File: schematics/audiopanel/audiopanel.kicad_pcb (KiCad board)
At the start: 2 copper layers, 29.2 x 21.6 mm, 3 parts, among them J1 Audio IN, J2 Audio OUT, J3 Conn

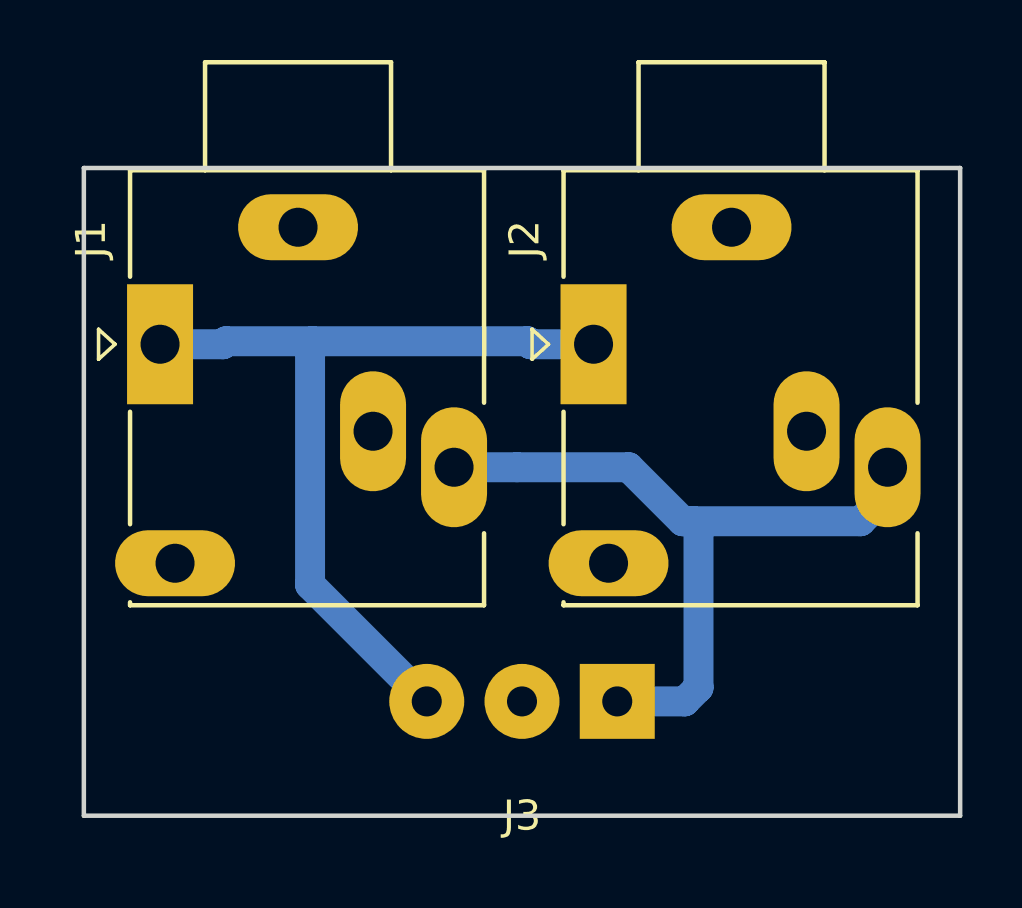
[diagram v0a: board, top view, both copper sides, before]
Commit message: Updated PCB for audio connectors
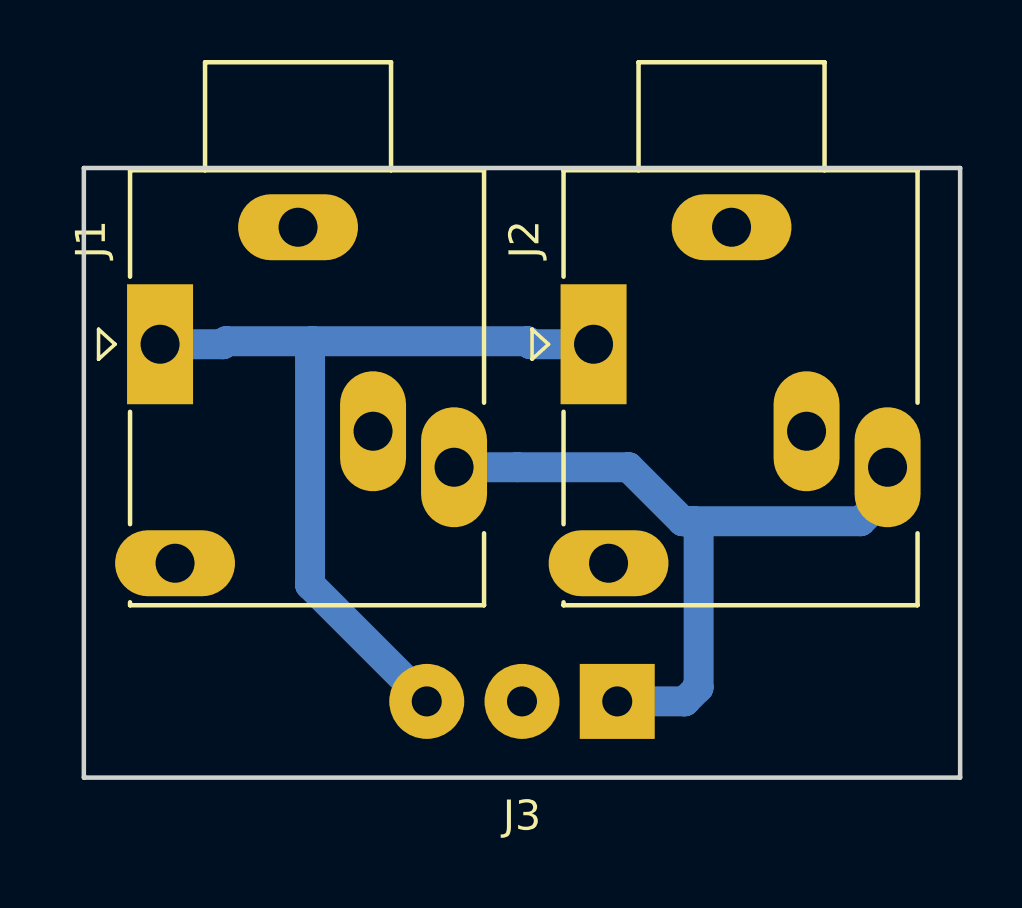
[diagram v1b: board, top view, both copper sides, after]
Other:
- board size 29.2 x 21.6 mm -> 29.2 x 20.3 mm
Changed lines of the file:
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@@
     (last_trace_width 1)
     (trace_clearance 0.5)
-    (zone_clearance 0.508)
+    (zone_clearance 0.2)
     (zone_45_only no)
     (trace_min 0.2)
@@
   )
   (dimension 29.21 (width 0.3) (layer Dwgs.User)
-    (gr_text "29,210 mm" (at 70.485 85.92) (layer Dwgs.User)
+    (gr_text "29,210 mm" (at 70.485 84.65) (layer Dwgs.User)
       (effects (font (size 1.5 1.5) (thickness 0.3)))
     )
-    (feature1 (pts (xy 85.09 78.74) (xy 85.09 84.406421)))
-    (feature2 (pts (xy 55.88 78.74) (xy 55.88 84.406421)))
-    (crossbar (pts (xy 55.88 83.82) (xy 85.09 83.82)))
-    (arrow1a (pts (xy 85.09 83.82) (xy 83.963496 84.406421)))
-    (arrow1b (pts (xy 85.09 83.82) (xy 83.963496 83.233579)))
-    (arrow2a (pts (xy 55.88 83.82) (xy 57.006504 84.406421)))
-    (arrow2b (pts (xy 55.88 83.82) (xy 57.006504 83.233579)))
-  )
-  (dimension 21.59 (width 0.3) (layer Dwgs.User)
-    (gr_text "21,590 mm" (at 48.7 67.945 90) (layer Dwgs.User)
+    (feature1 (pts (xy 85.09 77.47) (xy 85.09 83.136421)))
+    (feature2 (pts (xy 55.88 77.47) (xy 55.88 83.136421)))
+    (crossbar (pts (xy 55.88 82.55) (xy 85.09 82.55)))
+    (arrow1a (pts (xy 85.09 82.55) (xy 83.963496 83.136421)))
+    (arrow1b (pts (xy 85.09 82.55) (xy 83.963496 81.963579)))
+    (arrow2a (pts (xy 55.88 82.55) (xy 57.006504 83.136421)))
+    (arrow2b (pts (xy 55.88 82.55) (xy 57.006504 81.963579)))
+  )
+  (dimension 20.32 (width 0.3) (layer Dwgs.User)
+    (gr_text "20,320 mm" (at 48.7 67.31 90) (layer Dwgs.User)
       (effects (font (size 1.5 1.5) (thickness 0.3)))
     )
     (feature1 (pts (xy 55.88 57.15) (xy 50.213579 57.15)))
-    (feature2 (pts (xy 55.88 78.74) (xy 50.213579 78.74)))
-    (crossbar (pts (xy 50.8 78.74) (xy 50.8 57.15)))
+    (feature2 (pts (xy 55.88 77.47) (xy 50.213579 77.47)))
+    (crossbar (pts (xy 50.8 77.47) (xy 50.8 57.15)))
     (arrow1a (pts (xy 50.8 57.15) (xy 51.386421 58.276504)))
     (arrow1b (pts (xy 50.8 57.15) (xy 50.213579 58.276504)))
-    (arrow2a (pts (xy 50.8 78.74) (xy 51.386421 77.613496)))
-    (arrow2b (pts (xy 50.8 78.74) (xy 50.213579 77.613496)))
-  )
-  (gr_line (start 55.88 78.74) (end 55.88 57.15) (layer Edge.Cuts) (width 0.15))
-  (gr_line (start 85.09 78.74) (end 55.88 78.74) (layer Edge.Cuts) (width 0.15))
-  (gr_line (start 85.09 57.15) (end 85.09 78.74) (layer Edge.Cuts) (width 0.15))
+    (arrow2a (pts (xy 50.8 77.47) (xy 51.386421 76.343496)))
+    (arrow2b (pts (xy 50.8 77.47) (xy 50.213579 76.343496)))
+  )
+  (gr_line (start 55.88 77.47) (end 55.88 57.15) (layer Edge.Cuts) (width 0.15))
+  (gr_line (start 85.09 77.47) (end 55.88 77.47) (layer Edge.Cuts) (width 0.15))
+  (gr_line (start 85.09 57.15) (end 85.09 77.47) (layer Edge.Cuts) (width 0.15))
   (gr_line (start 55.88 57.15) (end 85.09 57.15) (layer Edge.Cuts) (width 0.15))
   (segment (start 70.32 67.125001) (end 68.22 67.125001) (width 1) (layer B.Cu) (net 2))
@@
   (segment (start 63.5 62.924991) (end 70.66999 62.924991) (width 1) (layer B.Cu) (net 3))
   (zone (net 1) (net_name "Net-(J1-PadS)") (layer B.Cu) (hatch edge 0.508)
-    (connect_pads (clearance 0.508))
+    (connect_pads (clearance 0.2))
     (min_thickness 0.254)
     (fill yes (arc_segments 16) (thermal_gap 0.508) (thermal_bridge_width 0.508))
     (polygon
       (pts
-        (xy 55.88 57.15) (xy 85.09 57.15) (xy 85.09 78.74) (xy 55.88 78.74)
+        (xy 55.88 57.15) (xy 85.09 57.15) (xy 85.09 77.47) (xy 55.88 77.47)
       )
     )
